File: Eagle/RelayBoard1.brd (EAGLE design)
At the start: 100 x 80 mm, 12 parts, among them IC1 ULN2003AN, K1 4052, K2 4052, K3 4051, X1 MKDSN1,5/6-5,08, X2 MKDSN1,5/6-5,08, X3 Con1, X4 MKDSN1,5/3-5,08, X7 Con2

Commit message: - some modifications, corrections, ...
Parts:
- X3: value Con1 -> CON1; device con-molex:KK-156-9 -> con-molex:KK-156-8
- X7: value Con2 -> CON2
- moved X3 2.54 mm to (25.4, 72.4)
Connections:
- net +5V: no longer X3.1
- net 0V: now also X3.8; no longer X3.9
- net N$18: now also X3.1; no longer X3.2
- net N$19: now also X3.2; no longer X3.3
- net N$20: now also X3.3; no longer X3.4
- net N$21: now also X3.4; no longer X3.5
- net N$22: now also X3.5; no longer X3.6
- net N$23: now also X3.6; no longer X3.7
- net N$24: now also X3.7; no longer X3.8
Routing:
- net 0V: track 123.3 -> 127.7 mm
- net N$20: track 15.2 -> 17.5 mm
- net N$21: track 14.5 -> 16.8 mm
- net N$18: track 16.5 -> 18.8 mm
- net N$19: track 15.8 -> 18.1 mm
- net N$22: track 14.1 -> 16.1 mm
- net N$23: track 14.8 -> 16.5 mm
- net N$24: track 17.0 -> 15.5 mm
- net +5V: track 22.9 -> 22.2 mm
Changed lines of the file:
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@@
 </element>
 <element name="C1" library="resistor" package="C025-025X050" value="100nF" x="6.35" y="54.61" rot="R90"/>
-<element name="X3" library="con-molex" package="KK-156-9" value="Con1" x="22.86" y="72.39" rot="R180">
-<attribute name="OC_NEWARK" value="unknown" x="-10.16" y="142.24" size="1.778" layer="27" rot="R180" display="off"/>
-<attribute name="MPN" value="" x="-10.16" y="142.24" size="1.778" layer="27" rot="R180" display="off"/>
-<attribute name="MF" value="" x="-10.16" y="142.24" size="1.778" layer="27" rot="R180" display="off"/>
-<attribute name="OC_FARNELL" value="unknown" x="-10.16" y="142.24" size="1.778" layer="27" rot="R180" display="off"/>
-</element>
-<element name="X7" library="con-molex" package="KK-156-5" value="Con2" x="58.42" y="72.39" rot="R180">
+<element name="X7" library="con-molex" package="KK-156-5" value="CON2" x="58.42" y="72.39" rot="R180">
 <attribute name="OC_NEWARK" value="unknown" x="33.02" y="152.4" size="1.778" layer="27" rot="R180" display="off"/>
 <attribute name="MPN" value="" x="33.02" y="152.4" size="1.778" layer="27" rot="R180" display="off"/>
@@
 <attribute name="MF" value="" x="26.67" y="64.77" size="1.778" layer="27" rot="R180" display="off"/>
 <attribute name="OC_FARNELL" value="1792904" x="26.67" y="64.77" size="1.778" layer="27" rot="R180" display="off"/>
+</element>
+<element name="X3" library="con-molex" package="KK-156-8" value="CON1" x="25.4" y="72.39" rot="R180">
+<attribute name="OC_NEWARK" value="unknown" x="25.4" y="72.39" size="1.778" layer="27" rot="R180" display="off"/>
+<attribute name="MPN" value="" x="25.4" y="72.39" size="1.778" layer="27" rot="R180" display="off"/>
+<attribute name="MF" value="" x="25.4" y="72.39" size="1.778" layer="27" rot="R180" display="off"/>
+<attribute name="OC_FARNELL" value="unknown" x="25.4" y="72.39" size="1.778" layer="27" rot="R180" display="off"/>
 </element>
 </elements>
@@
 </signal>
 <signal name="+5V">
-<contactref element="X3" pad="1"/>
 <contactref element="X7" pad="3"/>
 <wire x1="43.18" y1="68.58" x2="39.37" y2="72.39" width="0.254" layer="16"/>
 <wire x1="54.61" y1="68.58" x2="43.18" y2="68.58" width="0.254" layer="16"/>
 <wire x1="58.42" y1="72.39" x2="54.61" y2="68.58" width="0.254" layer="16"/>
-<wire x1="39.37" y1="72.39" x2="38.7" y2="72.39" width="0.254" layer="16"/>
 </signal>
 <signal name="0V">
@@
 <contactref element="C1" pad="2"/>
 <contactref element="IC1" pad="8"/>
-<contactref element="X3" pad="9"/>
 <wire x1="8.89" y1="58.42" x2="6.35" y2="55.88" width="0.254" layer="16"/>
 <wire x1="11.43" y1="58.42" x2="8.89" y2="58.42" width="0.254" layer="16"/>
-<wire x1="7.62" y1="58.42" x2="7.62" y2="72.39" width="0.254" layer="16"/>
+<wire x1="7.62" y1="58.42" x2="7.62" y2="76.2" width="0.254" layer="16"/>
 <wire x1="8.89" y1="58.42" x2="7.62" y2="58.42" width="0.254" layer="16"/>
 <wire x1="54.46" y1="72.39" x2="50.5" y2="72.39" width="0.254" layer="1"/>
@@
 <wire x1="91.44" y1="66.04" x2="81.28" y2="76.2" width="0.254" layer="16"/>
 <wire x1="54.61" y1="72.39" x2="54.46" y2="72.39" width="0.254" layer="16"/>
-<wire x1="7.62" y1="76.2" x2="7.62" y2="72.39" width="0.254" layer="16"/>
-<wire x1="58.42" y1="76.2" x2="7.62" y2="76.2" width="0.254" layer="16"/>
-<wire x1="7.62" y1="72.39" x2="7.02" y2="72.39" width="0.254" layer="16"/>
+<wire x1="58.42" y1="76.2" x2="12.7" y2="76.2" width="0.254" layer="16"/>
+<contactref element="X3" pad="8"/>
+<wire x1="12.7" y1="76.2" x2="7.62" y2="76.2" width="0.254" layer="16"/>
+<wire x1="12.7" y1="76.2" x2="12.7" y2="72.39" width="0.254" layer="16"/>
+<wire x1="12.7" y1="72.39" x2="11.54" y2="72.39" width="0.254" layer="16"/>
 </signal>
 <signal name="N$18">
 <contactref element="IC1" pad="1"/>
-<contactref element="X3" pad="2"/>
-<wire x1="34.29" y1="63.5" x2="29.21" y2="58.42" width="0.254" layer="1"/>
-<wire x1="34.29" y1="72.39" x2="34.29" y2="63.5" width="0.254" layer="1"/>
-<wire x1="34.29" y1="72.39" x2="34.74" y2="72.39" width="0.254" layer="1"/>
+<contactref element="X3" pad="1"/>
+<wire x1="38.1" y1="67.31" x2="29.21" y2="58.42" width="0.254" layer="1"/>
+<wire x1="38.1" y1="72.39" x2="38.1" y2="67.31" width="0.254" layer="1"/>
+<wire x1="38.1" y1="72.39" x2="39.26" y2="72.39" width="0.254" layer="1"/>
 </signal>
 <signal name="N$19">
 <contactref element="IC1" pad="2"/>
-<contactref element="X3" pad="3"/>
-<wire x1="30.48" y1="62.23" x2="26.67" y2="58.42" width="0.254" layer="1"/>
-<wire x1="30.48" y1="72.39" x2="30.48" y2="62.23" width="0.254" layer="1"/>
-<wire x1="30.48" y1="72.39" x2="30.78" y2="72.39" width="0.254" layer="1"/>
+<contactref element="X3" pad="2"/>
+<wire x1="34.29" y1="66.04" x2="26.67" y2="58.42" width="0.254" layer="1"/>
+<wire x1="34.29" y1="72.39" x2="34.29" y2="66.04" width="0.254" layer="1"/>
+<wire x1="34.29" y1="72.39" x2="35.3" y2="72.39" width="0.254" layer="1"/>
 </signal>
 <signal name="N$20">
 <contactref element="IC1" pad="3"/>
-<contactref element="X3" pad="4"/>
-<wire x1="26.67" y1="60.96" x2="24.13" y2="58.42" width="0.254" layer="1"/>
-<wire x1="26.67" y1="72.39" x2="26.67" y2="60.96" width="0.254" layer="1"/>
-<wire x1="26.67" y1="72.39" x2="26.82" y2="72.39" width="0.254" layer="1"/>
+<contactref element="X3" pad="3"/>
+<wire x1="30.48" y1="64.77" x2="24.13" y2="58.42" width="0.254" layer="1"/>
+<wire x1="30.48" y1="72.39" x2="30.48" y2="64.77" width="0.254" layer="1"/>
+<wire x1="30.48" y1="72.39" x2="31.34" y2="72.39" width="0.254" layer="1"/>
 </signal>
 <signal name="N$21">
 <contactref element="IC1" pad="4"/>
-<contactref element="X3" pad="5"/>
-<wire x1="22.86" y1="59.69" x2="21.59" y2="58.42" width="0.254" layer="1"/>
-<wire x1="22.86" y1="72.39" x2="22.86" y2="59.69" width="0.254" layer="1"/>
+<contactref element="X3" pad="4"/>
+<wire x1="26.67" y1="63.5" x2="21.59" y2="58.42" width="0.254" layer="1"/>
+<wire x1="26.67" y1="72.39" x2="26.67" y2="63.5" width="0.254" layer="1"/>
+<wire x1="26.67" y1="72.39" x2="27.38" y2="72.39" width="0.254" layer="1"/>
 </signal>
 <signal name="N$22">
 <contactref element="IC1" pad="5"/>
-<contactref element="X3" pad="6"/>
-<wire x1="19.05" y1="72.39" x2="19.05" y2="58.42" width="0.254" layer="1"/>
-<wire x1="19.05" y1="72.39" x2="18.9" y2="72.39" width="0.254" layer="1"/>
+<contactref element="X3" pad="5"/>
+<wire x1="22.86" y1="62.23" x2="19.05" y2="58.42" width="0.254" layer="1"/>
+<wire x1="22.86" y1="72.39" x2="22.86" y2="62.23" width="0.254" layer="1"/>
+<wire x1="22.86" y1="72.39" x2="23.42" y2="72.39" width="0.254" layer="1"/>
 </signal>
 <signal name="N$23">
 <contactref element="IC1" pad="6"/>
-<contactref element="X3" pad="7"/>
 <wire x1="15.24" y1="59.69" x2="16.51" y2="58.42" width="0.254" layer="1"/>
-<wire x1="15.24" y1="72.39" x2="15.24" y2="59.69" width="0.254" layer="1"/>
-<wire x1="15.24" y1="72.39" x2="14.94" y2="72.39" width="0.254" layer="1"/>
+<contactref element="X3" pad="6"/>
+<wire x1="19.05" y1="63.5" x2="15.24" y2="59.69" width="0.254" layer="1"/>
+<wire x1="19.05" y1="72.39" x2="19.05" y2="63.5" width="0.254" layer="1"/>
+<wire x1="19.05" y1="72.39" x2="19.46" y2="72.39" width="0.254" layer="1"/>
 </signal>
 <signal name="N$24">
 <contactref element="IC1" pad="7"/>
-<contactref element="X3" pad="8"/>
-<wire x1="10.98" y1="72.39" x2="11.43" y2="72.39" width="0.4064" layer="16"/>
-<wire x1="11.43" y1="72.39" x2="11.43" y2="64.77" width="0.4064" layer="16"/>
-<wire x1="11.43" y1="64.77" x2="13.97" y2="64.77" width="0.4064" layer="16"/>
-<wire x1="13.97" y1="64.77" x2="13.97" y2="58.42" width="0.4064" layer="16"/>
+<contactref element="X3" pad="7"/>
+<wire x1="13.97" y1="72.39" x2="13.97" y2="58.42" width="0.254" layer="16"/>
+<wire x1="15.5" y1="72.39" x2="13.97" y2="72.39" width="0.254" layer="16"/>
 </signal>
 <signal name="+12V">

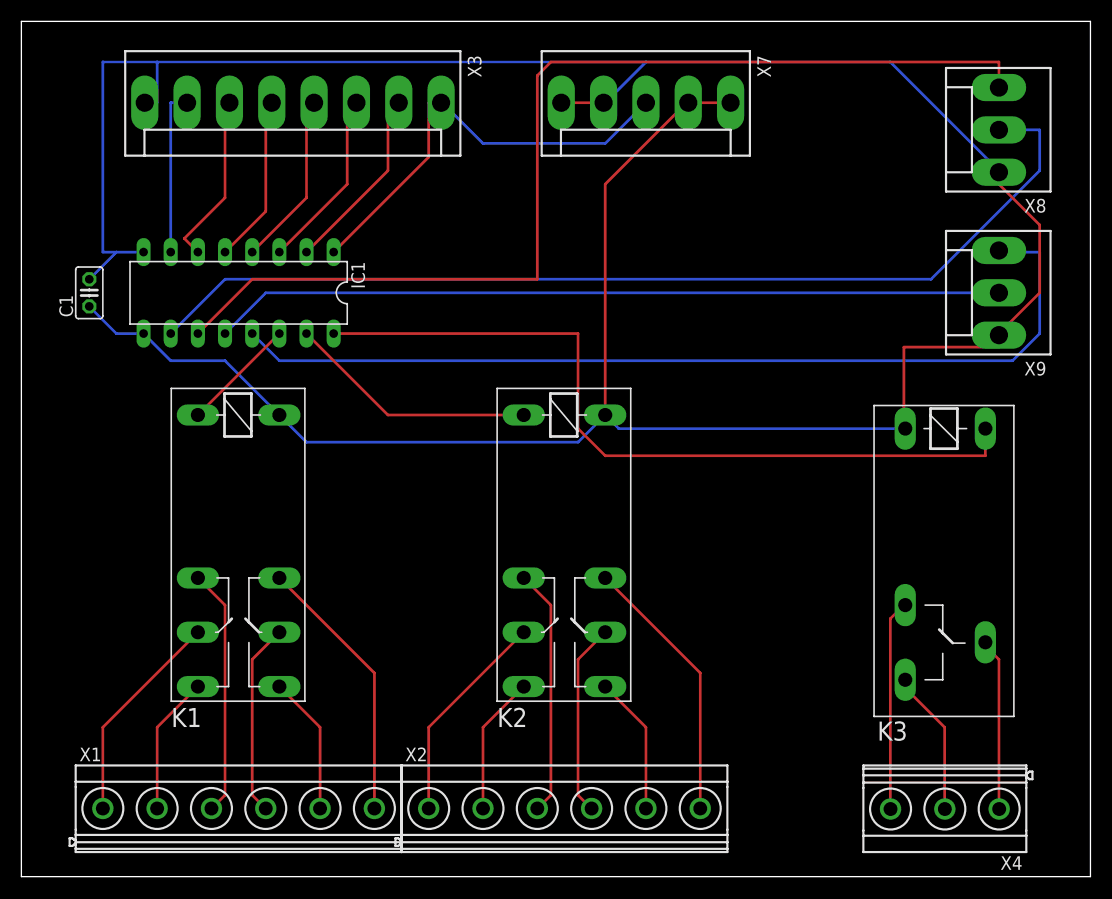
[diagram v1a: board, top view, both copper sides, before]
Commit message: - corrections for RelayBoard1:   - using right connectors from library con-molex   - single sided routing - corrections for ButtonBoard:   - using right connector from library con-molex   - using right switches from library switch-misc (SRK/SRKL) - component placement & board layout for ButtonBoard done - CPUBoard:   - some components moved around the board   - re-routing (partially)
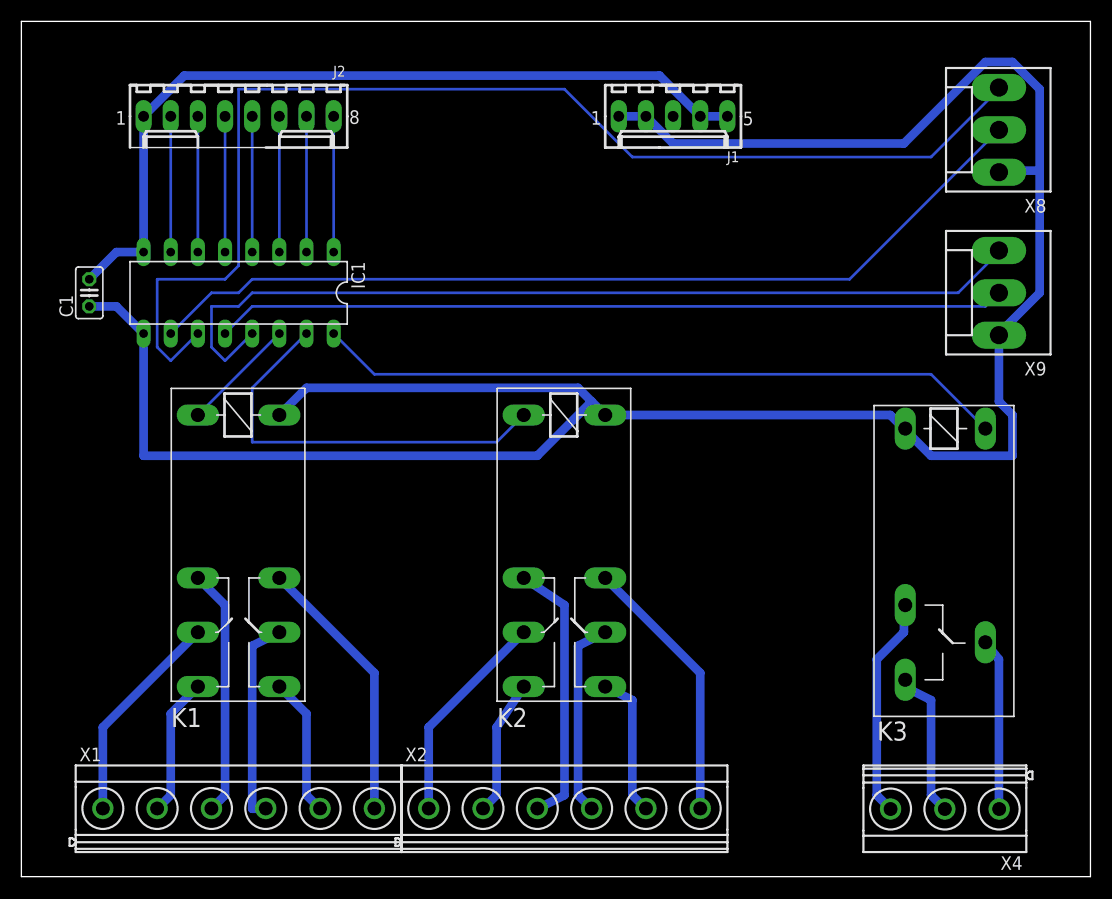
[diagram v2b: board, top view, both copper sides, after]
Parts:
- removed X3: CON1, con-molex:KK-156-8
- removed X7: CON2, con-molex:KK-156-5
- added J1: POWER, con-molex:6410-05
- added J2: CPU_BOARD, con-molex:6410-08
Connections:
- removed net N$24: IC1.7, X3.7
- new net N$5: IC1.1, J2.8
- net +12V: now also J1.1, J1.2; no longer X7.1, X7.2
- net +5V: now also J1.3; no longer X7.3
- net 0V: now also J1.4, J1.5, J2.1; no longer X3.8, X7.4, X7.5
- net N$18: now also IC1.2, J2.7; no longer IC1.1, X3.1
- net N$19: now also IC1.3, J2.6; no longer IC1.2, X3.2
- net N$20: now also IC1.4, J2.5; no longer IC1.3, X3.3
- net N$21: now also IC1.5, J2.4; no longer IC1.4, X3.4
- net N$22: now also IC1.6, J2.3; no longer IC1.5, X3.5
- net N$23: now also IC1.7, J2.2; no longer IC1.6, X3.6
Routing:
- net +12V: track 155.8 -> 219.1 mm
- net 0V: track 127.7 -> 76.6 mm
- net +5V: track 22.2 -> 0.00 mm
- net N$24: track 15.5 -> 0.00 mm
- net N$25: track 23.5 -> 38.7 mm
- net N$27: track 99.0 -> 112.9 mm
- net N$5: track 0.00 -> 12.7 mm
- net N$28: track 95.2 -> 85.4 mm
- net N$4: track 73.4 -> 64.6 mm
- net N$18: track 18.8 -> 12.7 mm
- net N$19: track 18.1 -> 12.7 mm
- net N$20: track 17.5 -> 12.7 mm
- net N$21: track 16.8 -> 12.7 mm
- net N$23: track 16.5 -> 12.7 mm
- net N$22: track 16.1 -> 12.7 mm
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
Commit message: - cabling of RelayBoard1 partly changed - some pin-swaps to ButtonBoard -> blrtest.c finally works as expected
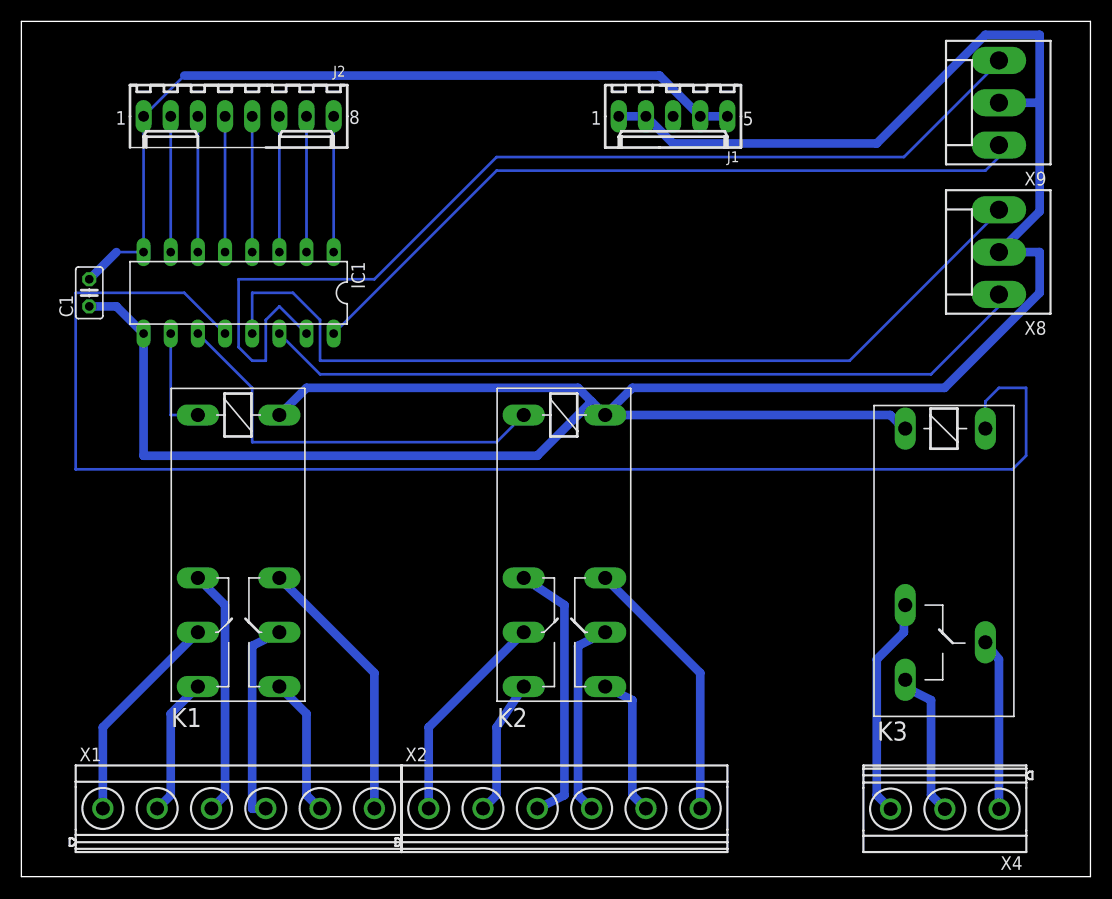
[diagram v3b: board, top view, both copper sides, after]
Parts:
- moved X9 17.8 mm to (91.4, 72.4)
- moved X8 11.4 mm to (91.4, 58.4)
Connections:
- net N$20 renamed REL4
- net N$21 renamed REL3
- net N$22 renamed REL2
- net N$23 renamed REL1
- net +12V: now also X8.2, X9.2; no longer X8.1, X9.1
- net N$25: now also IC1.11; no longer IC1.15
- net N$26: now also IC1.12, K3.2; no longer IC1.14, K1.2
- net N$27: now also IC1.14, X8.1; no longer IC1.11, X8.3
- net N$28: now also IC1.13, X8.3; no longer IC1.10, X8.2
- net N$29: now also IC1.16, X9.1; no longer IC1.13, X9.3
- net N$30: now also IC1.15, X9.3; no longer IC1.12, X9.2
- net N$4: now also IC1.10, K1.2; no longer IC1.16, K3.2
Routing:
- net N$26: track 10.8 -> 134.7 mm
- net N$4: track 64.6 -> 10.2 mm
- net N$27: track 112.9 -> 72.6 mm
- net +12V: track 219.1 -> 246.2 mm
- net N$30: track 74.0 -> 98.3 mm
- net N$29: track 85.1 -> 70.2 mm
- net N$28: track 85.4 -> 84.5 mm
